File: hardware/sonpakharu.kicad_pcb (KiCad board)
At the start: 2 copper layers, 51.3 x 71.1 mm, 62 parts, among them IC1 ESP32-S3-WROOM-1U-N4, J1 ADC4, J10 EXT2, J11 EXT3, J12 BATT, J13 EXT7, J14 PWR, J15 EXT8, J16 FTDI, J17 485, J2 ADC3, J3 ADC2, J4 ADC1, J5 EXT4, J6 I2C, J7 EXT5, J8 EXT1, J9 EXT6, Q1 DMG3415U, Q2 S8050, Q3 S8050, Q4 S8050, SW1 Boot, SW2 Reset, U1 AP2112K-3.3TRG1, U2 MCP73831-2-OT, U3 ADS1115IDGSR, U4 MAX485E

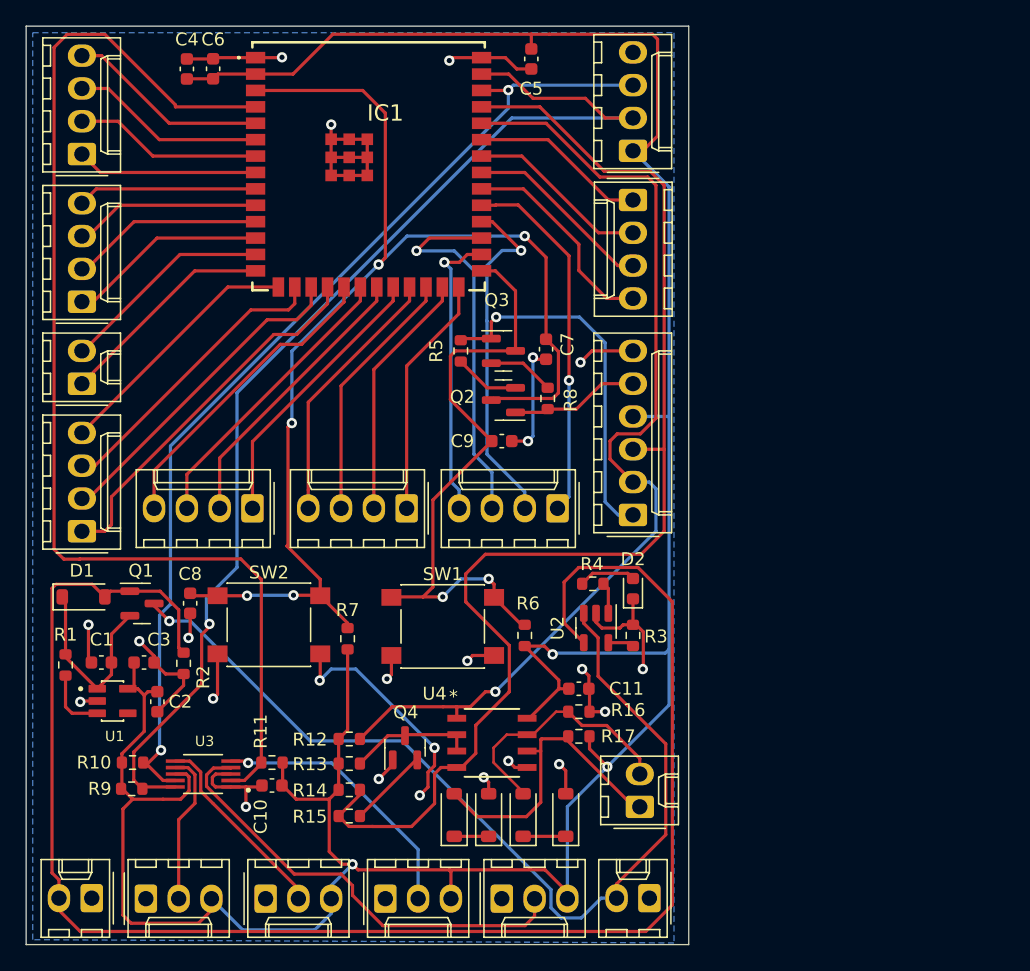
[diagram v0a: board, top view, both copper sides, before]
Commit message: all tracks corrected, 0 errors 0 warnings
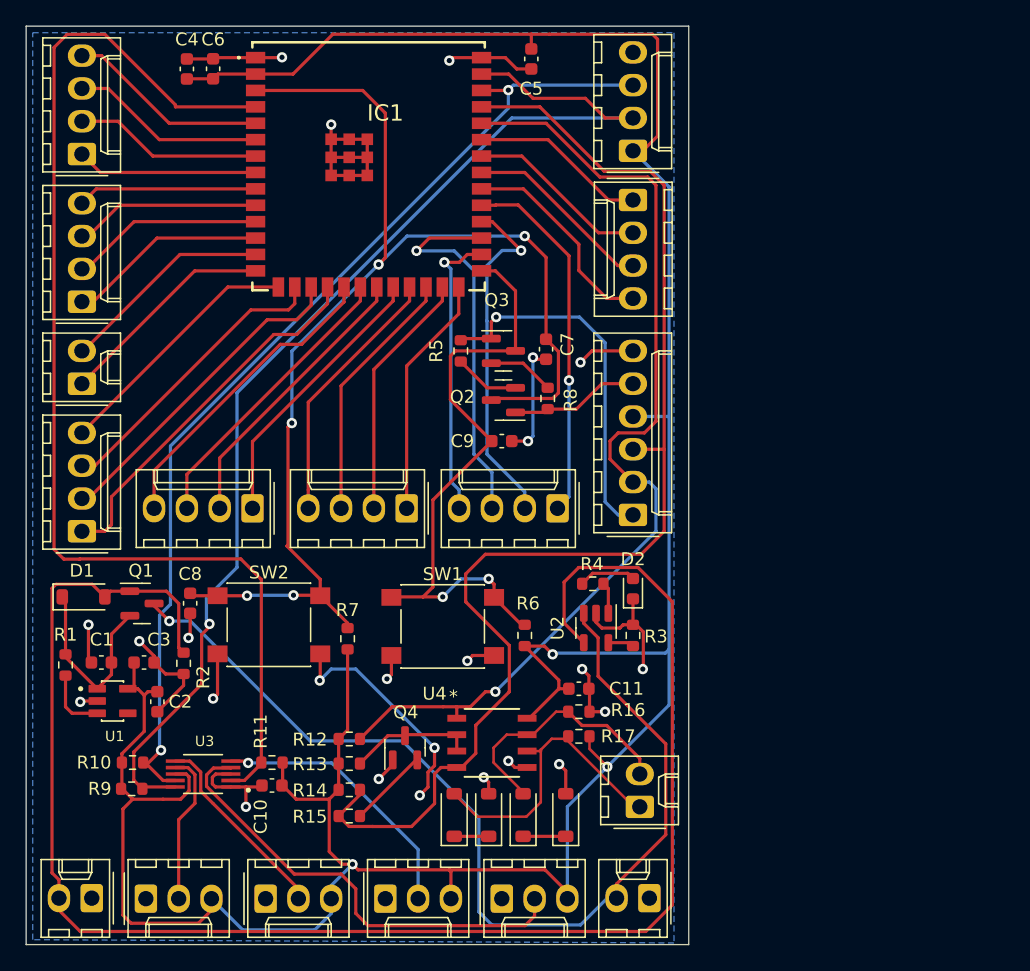
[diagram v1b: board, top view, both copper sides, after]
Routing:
- net +BATT: track 73.7 -> 77.6 mm
- net /A0: track 35.0 -> 35.7 mm

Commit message: Added: labels
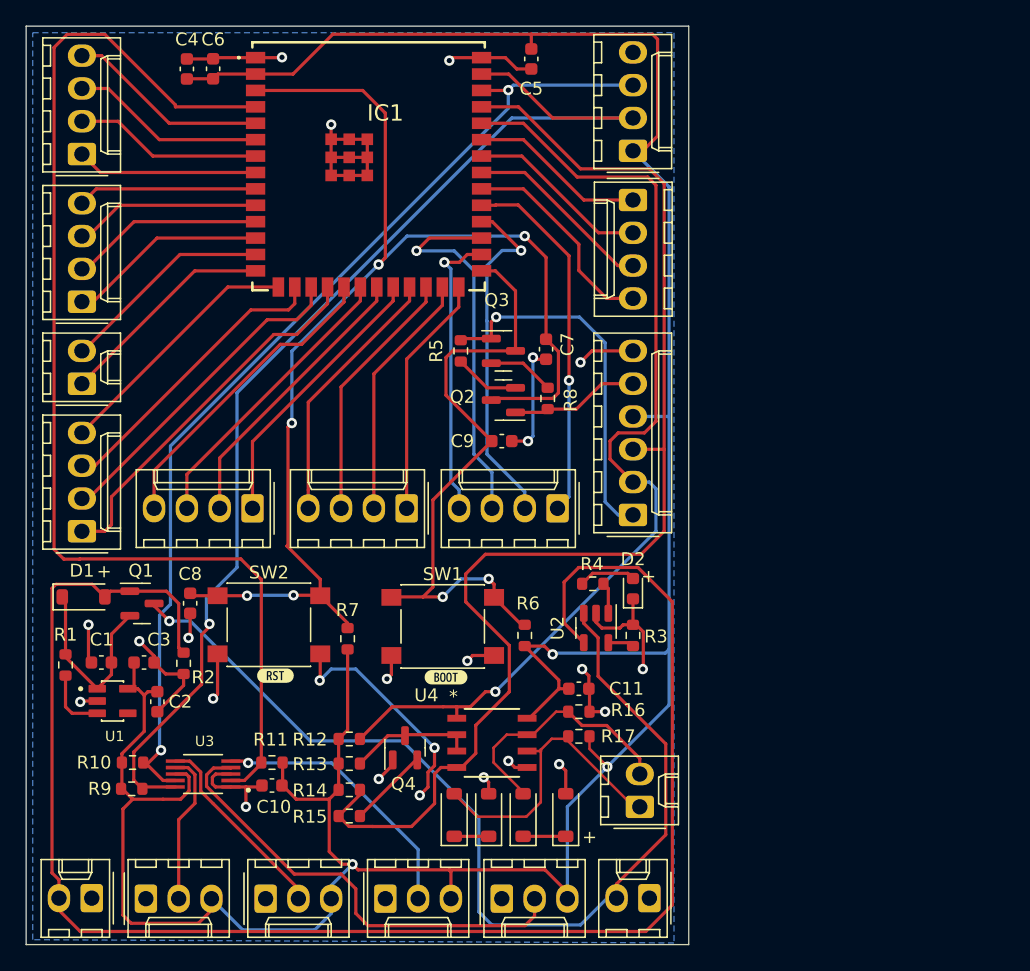
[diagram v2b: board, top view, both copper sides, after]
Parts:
- added kibuzzard-659587E1: G***, kibuzzard-659587E1, F.Cu at (125.2, 87.9)
- added kibuzzard-659587ED: G***, kibuzzard-659587ED, F.Cu at (138.4, 88.0)
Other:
- board text added: "+"

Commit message: completed all labels, added mx485 mpn
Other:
- board text added: "1"
- board text added: "10"
- board text added: "11"
- board text added: "12"
- board text added: "13"
- board text added: "14"
- board text added: "15"
- board text added: "16"
- board text added: "17"
- board text added: "18"
- board text added: "19"
- board text added: "2"
- board text added: "20"
- board text added: "21"
- board text added: "22"
- board text added: "23"
- board text added: "24"
- board text added: "25"
- board text added: "26"
- board text added: "27"
- board text added: "28"
- board text added: "29"
- board text added: "3"
- board text added: "30"
- board text added: "3V"
- board text added: "4"
- board text added: "5"
- board text added: "5V"
- board text added: "6"
- board text added: "7"
- board text added: "8"
- board text added: "9"
- board text added: "A1"
- board text added: "A2"
- board text added: "A3"
- board text added: "BAT+"
- board text added: "D+"
- board text added: "D-"
- board text added: "DT"
- board text added: "G"
- board text added: "RT"
- board text added: "RX"
- board text added: "SCL"
- board text added: "SDA"
- board text added: "TX"
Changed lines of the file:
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@@
     (property "ki_keywords" "connector")
     (attr through_hole)
-    (fp_text reference "J14" (at 1.016 4.064) (layer "B.SilkS")
+    (fp_text reference "J14" (at 1.016 4.532) (layer "B.SilkS")
         (effects (font (size 1 1) (thickness 0.15)) (justify mirror))
     )
@@
     (at 141.986 93.091)
     (tags "MAX485ESA+ ")
+    (property "MPN" "C19738")
     (property "Sheetfile" "sonpakharu.kicad_sch")
     (property "Sheetname" "")
@@
     (property "ki_keywords" "connector")
     (attr through_hole)
-    (fp_text reference "J1" (at 2.54 -4.12) (layer "B.SilkS")
+    (fp_text reference "J1" (at 2.794 -4.572) (layer "B.SilkS")
         (effects (font (size 1 1) (thickness 0.15)) (justify mirror))
     )
@@
     (attr board_only exclude_from_pos_files exclude_from_bom)
     (fp_text reference "kibuzzard-659587E1" (at 0 -3.603625) (layer "F.SilkS") hide
-        (effects (font (size 0 0)))
+        (effects (font (size 0 0) (thickness 0.15)))
     )
     (fp_text value "G***" (at 0 3.603625) (layer "F.SilkS") hide
-        (effects (font (size 0 0)))
+        (effects (font (size 0 0) (thickness 0.15)))
     )
     (fp_poly
@@
     (attr board_only exclude_from_pos_files exclude_from_bom)
     (fp_text reference "kibuzzard-659587ED" (at 0 -3.603625) (layer "F.SilkS") hide
-        (effects (font (size 0 0)))
+        (effects (font (size 0 0) (thickness 0.15)))
     )
     (fp_text value "G***" (at 0 3.603625) (layer "F.SilkS") hide
-        (effects (font (size 0 0)))
+        (effects (font (size 0 0) (thickness 0.15)))
     )
     (fp_poly
@@
   (gr_rect (start 105.918 37.592) (end 157.226 108.712)
     (stroke (width 0.05) (type default)) (fill none) (layer "Edge.Cuts"))
+  (gr_text "5V" (at 109.22 108.077) (layer "B.SilkS")
+    (effects (font (size 1 1) (thickness 0.1)) (justify left bottom mirror))
+  )
+  (gr_text "G" (at 124.841 107.95) (layer "B.SilkS")
+    (effects (font (size 1 1) (thickness 0.1)) (justify left bottom mirror))
+  )
+  (gr_text "3V" (at 121.158 108.077) (layer "B.SilkS")
+    (effects (font (size 1 1) (thickness 0.1)) (justify left bottom mirror))
+  )
+  (gr_text "1" (at 108.077 39.37 90) (layer "B.SilkS")
+    (effects (font (size 1 1) (thickness 0.1)) (justify left bottom mirror))
+  )
+  (gr_text "G" (at 155.829 38.227 90) (layer "B.SilkS")
+    (effects (font (size 1 1) (thickness 0.1)) (justify left bottom mirror))
+  )
+  (gr_text "D+" (at 156.337 97.155 90) (layer "B.SilkS")
+    (effects (font (size 1 1) (thickness 0.1)) (justify left bottom mirror))
+  )
+  (gr_text "RT" (at 155.702 64.262 90) (layer "B.SilkS")
+    (effects (font (size 1 1) (thickness 0.1)) (justify left bottom mirror))
+  )
+  (gr_text "26" (at 146.177 76.835 180) (layer "B.SilkS")
+    (effects (font (size 1 1) (thickness 0.1)) (justify left bottom mirror))
+  )
+  (gr_text "9" (at 108.204 62.103 90) (layer "B.SilkS")
+    (effects (font (size 1 1) (thickness 0.1)) (justify left bottom mirror))
+  )
+  (gr_text "G" (at 133.985 107.95) (layer "B.SilkS")
+    (effects (font (size 1 1) (thickness 0.1)) (justify left bottom mirror))
+  )
+  (gr_text "13" (at 108.077 73.152 90) (layer "B.SilkS")
+    (effects (font (size 1 1) (thickness 0.1)) (justify left bottom mirror))
+  )
+  (gr_text "5" (at 108.204 50.8 90) (layer "B.SilkS")
+    (effects (font (size 1 1) (thickness 0.1)) (justify left bottom mirror))
+  )
+  (gr_text "A1" (at 146.05 108.204) (layer "B.SilkS")
+    (effects (font (size 1 1) (thickness 0.1)) (justify left bottom mirror))
+  )
+  (gr_text "21" (at 131.953 76.835 180) (layer "B.SilkS")
+    (effects (font (size 1 1) (thickness 0.1)) (justify left bottom mirror))
+  )
+  (gr_text "15" (at 114.808 76.835 180) (layer "B.SilkS")
+    (effects (font (size 1 1) (thickness 0.1)) (justify left bottom mirror))
+  )
+  (gr_text "TX" (at 155.829 69.469 90) (layer "B.SilkS")
+    (effects (font (size 1 1) (thickness 0.1)) (justify left bottom mirror))
+  )
+  (gr_text "8" (at 108.204 58.674 90) (layer "B.SilkS")
+    (effects (font (size 1 1) (thickness 0.1)) (justify left bottom mirror))
+  )
+  (gr_text "3V" (at 139.7 108.077) (layer "B.SilkS")
+    (effects (font (size 1 1) (thickness 0.1)) (justify left bottom mirror))
+  )
+  (gr_text "3V" (at 130.556 108.077) (layer "B.SilkS")
+    (effects (font (size 1 1) (thickness 0.1)) (justify left bottom mirror))
+  )
+  (gr_text "29" (at 155.956 52.578 90) (layer "B.SilkS")
+    (effects (font (size 1 1) (thickness 0.1)) (justify left bottom mirror))
+  )
+  (gr_text "SDA" (at 155.829 40.259 90) (layer "B.SilkS")
+    (effects (font (size 1 1) (thickness 0.1)) (justify left bottom mirror))
+  )
+  (gr_text "20" (at 129.286 76.708 180) (layer "B.SilkS")
+    (effects (font (size 1 1) (thickness 0.1)) (justify left bottom mirror))
+  )
+  (gr_text "3" (at 108.204 44.45 90) (layer "B.SilkS")
+    (effects (font (size 1 1) (thickness 0.1)) (justify left bottom mirror))
+  )
+  (gr_text "SCL" (at 155.829 43.307 90) (layer "B.SilkS")
+    (effects (font (size 1 1) (thickness 0.1)) (justify left bottom mirror))
+  )
+  (gr_text "3V" (at 155.702 66.802 90) (layer "B.SilkS")
+    (effects (font (size 1 1) (thickness 0.1)) (justify left bottom mirror))
+  )
+  (gr_text "19" (at 126.619 76.835 180) (layer "B.SilkS")
+    (effects (font (size 1 1) (thickness 0.1)) (justify left bottom mirror))
+  )
+  (gr_text "17" (at 119.888 76.835 180) (layer "B.SilkS")
+    (effects (font (size 1 1) (thickness 0.1)) (justify left bottom mirror))
+  )
+  (gr_text "D-" (at 156.337 94.488 90) (layer "B.SilkS")
+    (effects (font (size 1 1) (thickness 0.1)) (justify left bottom mirror))
+  )
+  (gr_text "A3" (at 118.491 108.077) (layer "B.SilkS")
+    (effects (font (size 1 1) (thickness 0.1)) (justify left bottom mirror))
+  )
+  (gr_text "10" (at 108.204 64.897 90) (layer "B.SilkS")
+    (effects (font (size 1 1) (thickness 0.1)) (justify left bottom mirror))
+  )
+  (gr_text "DT" (at 156.083 74.422 90) (layer "B.SilkS")
+    (effects (font (size 1 1) (thickness 0.1)) (justify left bottom mirror))
+  )
+  (gr_text "G" (at 154.813 108.077) (layer "B.SilkS")
+    (effects (font (size 1 1) (thickness 0.1)) (justify left bottom mirror))
+  )
+  (gr_text "12" (at 108.077 70.612 90) (layer "B.SilkS")
+    (effects (font (size 1 1) (thickness 0.1)) (justify left bottom mirror))
+  )
+  (gr_text "22" (at 134.493 76.835 180) (layer "B.SilkS")
+    (effects (font (size 1 1) (thickness 0.1)) (justify left bottom mirror))
+  )
+  (gr_text "BAT+" (at 153.416 108.077) (layer "B.SilkS")
+    (effects (font (size 1 1) (thickness 0.1)) (justify left bottom mirror))
+  )
+  (gr_text "3V" (at 148.59 108.204) (layer "B.SilkS")
+    (effects (font (size 1 1) (thickness 0.1)) (justify left bottom mirror))
+  )
+  (gr_text "23" (at 138.303 76.835 180) (layer "B.SilkS")
+    (effects (font (size 1 1) (thickness 0.1)) (justify left bottom mirror))
+  )
+  (gr_text "G" (at 115.443 108.077) (layer "B.SilkS")
+    (effects (font (size 1 1) (thickness 0.1)) (justify left bottom mirror))
+  )
+  (gr_text "18" (at 122.555 76.835 180) (layer "B.SilkS")
+    (effects (font (size 1 1) (thickness 0.1)) (justify left bottom mirror))
+  )
+  (gr_text "16" (at 117.475 76.835 180) (layer "B.SilkS")
+    (effects (font (size 1 1) (thickness 0.1)) (justify left bottom mirror))
+  )
+  (gr_text "G" (at 142.875 108.077) (layer "B.SilkS")
+    (effects (font (size 1 1) (thickness 0.1)) (justify left bottom mirror))
+  )
+  (gr_text "24" (at 140.97 76.835 180) (layer "B.SilkS")
+    (effects (font (size 1 1) (thickness 0.1)) (justify left bottom mirror))
+  )
+  (gr_text "28" (at 155.956 55.118 90) (layer "B.SilkS")
+    (effects (font (size 1 1) (thickness 0.1)) (justify left bottom mirror))
+  )
+  (gr_text "7" (at 108.204 56.007 90) (layer "B.SilkS")
+    (effects (font (size 1 1) (thickness 0.1)) (justify left bottom mirror))
+  )
+  (gr_text "A1" (at 137.033 108.077) (layer "B.SilkS")
+    (effects (font (size 1 1) (thickness 0.1)) (justify left bottom mirror))
+  )
+  (gr_text "RX" (at 155.956 72.009 90) (layer "B.SilkS")
+    (effects (font (size 1 1) (thickness 0.1)) (justify left bottom mirror))
+  )
+  (gr_text "25" (at 143.637 76.835 180) (layer "B.SilkS")
+    (effects (font (size 1 1) (thickness 0.1)) (justify left bottom mirror))
+  )
+  (gr_text "4" (at 108.204 46.863 90) (layer "B.SilkS")
+    (effects (font (size 1 1) (thickness 0.1)) (justify left bottom mirror))
+  )
+  (gr_text "27" (at 155.829 57.404 90) (layer "B.SilkS")
+    (effects (font (size 1 1) (thickness 0.1)) (justify left bottom mirror))
+  )
+  (gr_text "G" (at 111.379 108.077) (layer "B.SilkS")
+    (effects (font (size 1 1) (thickness 0.1)) (justify left bottom mirror))
+  )
+  (gr_text "A2" (at 127.762 107.95) (layer "B.SilkS")
+    (effects (font (size 1 1) (thickness 0.1)) (justify left bottom mirror))
+  )
+  (gr_text "11" (at 108.331 68.199 90) (layer "B.SilkS")
+    (effects (font (size 1 1) (thickness 0.1)) (justify left bottom mirror))
+  )
+  (gr_text "30" (at 155.956 50.165 90) (layer "B.SilkS")
+    (effects (font (size 1 1) (thickness 0.1)) (justify left bottom mirror))
+  )
+  (gr_text "6" (at 108.077 53.467 90) (layer "B.SilkS")
+    (effects (font (size 1 1) (thickness 0.1)) (justify left bottom mirror))
+  )
+  (gr_text "3V" (at 155.829 46.228 90) (layer "B.SilkS")
+    (effects (font (size 1 1) (thickness 0.1)) (justify left bottom mirror))
+  )
+  (gr_text "2" (at 108.204 42.037 90) (layer "B.SilkS")
+    (effects (font (size 1 1) (thickness 0.1)) (justify left bottom mirror))
+  )
+  (gr_text "G" (at 155.702 61.722 90) (layer "B.SilkS")
+    (effects (font (size 1 1) (thickness 0.1)) (justify left bottom mirror))
+  )
+  (gr_text "14" (at 108.077 75.692 90) (layer "B.SilkS")
+    (effects (font (size 1 1) (thickness 0.1)) (justify left bottom mirror))
+  )
   (gr_text "+" (at 153.543 80.772) (layer "F.SilkS")
     (effects (font (size 1 1) (thickness 0.1)) (justify left bottom))

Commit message: corrected labels
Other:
- board text added: "A0"
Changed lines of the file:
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@@
     (property "ki_keywords" "connector")
     (attr through_hole)
-    (fp_text reference "J17" (at 5.461 1.758) (layer "B.SilkS")
+    (fp_text reference "J17" (at 1.524 -4.465 90) (layer "B.SilkS")
         (effects (font (size 1 1) (thickness 0.15)) (justify mirror))
     )
@@
     (effects (font (size 1 1) (thickness 0.1)) (justify left bottom mirror))
   )
-  (gr_text "G" (at 124.841 107.95) (layer "B.SilkS")
+  (gr_text "G" (at 124.841 108.077) (layer "B.SilkS")
     (effects (font (size 1 1) (thickness 0.1)) (justify left bottom mirror))
   )
@@
     (effects (font (size 1 1) (thickness 0.1)) (justify left bottom mirror))
   )
-  (gr_text "A1" (at 146.05 108.204) (layer "B.SilkS")
+  (gr_text "A0" (at 146.05 108.204) (layer "B.SilkS")
     (effects (font (size 1 1) (thickness 0.1)) (justify left bottom mirror))
   )
@@
     (effects (font (size 1 1) (thickness 0.1)) (justify left bottom mirror))
   )
-  (gr_text "A2" (at 127.762 107.95) (layer "B.SilkS")
-    (effects (font (size 1 1) (thickness 0.1)) (justify left bottom mirror))
-  )
+  (gr_text "A2" (at 127.762 108.077) (layer "B.SilkS")
+    (effects (font (size 1 1) (thickness 0.1)) (justify left bottom mirror))
+  )

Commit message: added holes
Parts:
- moved J17 3.18 mm to (153.6, 94.9)
- moved C4 1.19 mm to (119.0, 41.9)
- moved R17 1.09 mm to (147.8, 91.9)
- moved C6 1.09 mm to (120.8, 41.9)
- moved R16 0.97 mm to (147.8, 90.3)
- moved C11 0.92 mm to (147.8, 88.6)
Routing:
- net GND: track 113.1 -> 120.8 mm
- net +BATT: track 77.6 -> 81.3 mm
- net +3V3: track 235.2 -> 233.2 mm
- net /D-: track 19.7 -> 18.2 mm
- net /IO4: track 91.5 -> 92.2 mm
- net /D+: track 23.5 -> 23.0 mm
- net VBUS: track 127.8 -> 128.3 mm
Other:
- outline, holes or cut-outs redrawn
